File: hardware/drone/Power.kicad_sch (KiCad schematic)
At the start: 48 parts, among them U1 STM32N645I0, U13 LM5907, U3 TPS628303, U4 TPS7A2118PQWDSGRQ1, U5 TPS628303

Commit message: Implemented power mux to select between battery and usb c 5V
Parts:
- added C85: 2.2u, symbol Device:C
- added C86, C89: 100n, symbol Device:C
- added C87, C88: 33u, symbol Device:C
- added L13: 10u, symbol Device:L
- added R15: 53.6k, symbol Device:R
- added R16, R18, R22: 10.2k, symbol Device:R
- added R17: 51.1k, symbol Device:R
- added R19, R21, R23: 5k, symbol Device:R
- added R20: 23.7k, symbol Device:R
- added U16: LMR51635XFDDCR, Package_TO_SOT_SMD:SOT-23-6, symbol SoftDrone:LMR51635XFDDCR
- added U18: TPS2121, Package_TO_SOT_SMD:SOT-583-8, symbol SoftDrone:TPS2121
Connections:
- net GND: now also C85.2, C87.2, C88.2, C89.2, R16.2, R17.2, R19.2, R21.2, R23.2, U16.4 (GND), U18.3 (CP2), U18.9 (ST)
- net VSYS_5V: now also U18.1 (OUT), U18.8 (OUT)
- new net: R17.1, U18.10 (ILM)
- new net: C89.1, U18.11 (SS)
- new net: C86.1, U16.6 (CB)
- new net: C86.2, L13.1, U16.5 (SW)
- new net: R15.2, R16.1, U16.1 (FB)
- new net PMUX_OV1: R20.2, R21.1, U18.5 (OV1)
- new net PMUX_OV2: R22.2, R23.1, U18.4 (OV2)
- new net PMUX_PR1: R18.2, R19.1, U18.6 (PR1)
- new net VBAT: C85.1, U16.2 (EN), U16.3 (VIN)
- new net VSYS_5V_BAT: C87.1, C88.1, L13.2, R15.1, U18.2 (IN2)
- new net VSYS_5V_USBC: R18.1, R20.1, R22.1, U18.7 (IN1)
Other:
- note added: "5V Power Mux"
- moved on the sheet: C10, C11, C12, C13, C14, C15, C16, C17, C18, C19, C2, C20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

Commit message: cleanup
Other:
- note added: "6S VBAT -> 5V SMPS"
- moved on the sheet: C10, C11, C12, C16, C19, C2, C20, C21, C22, C23, C24, C25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

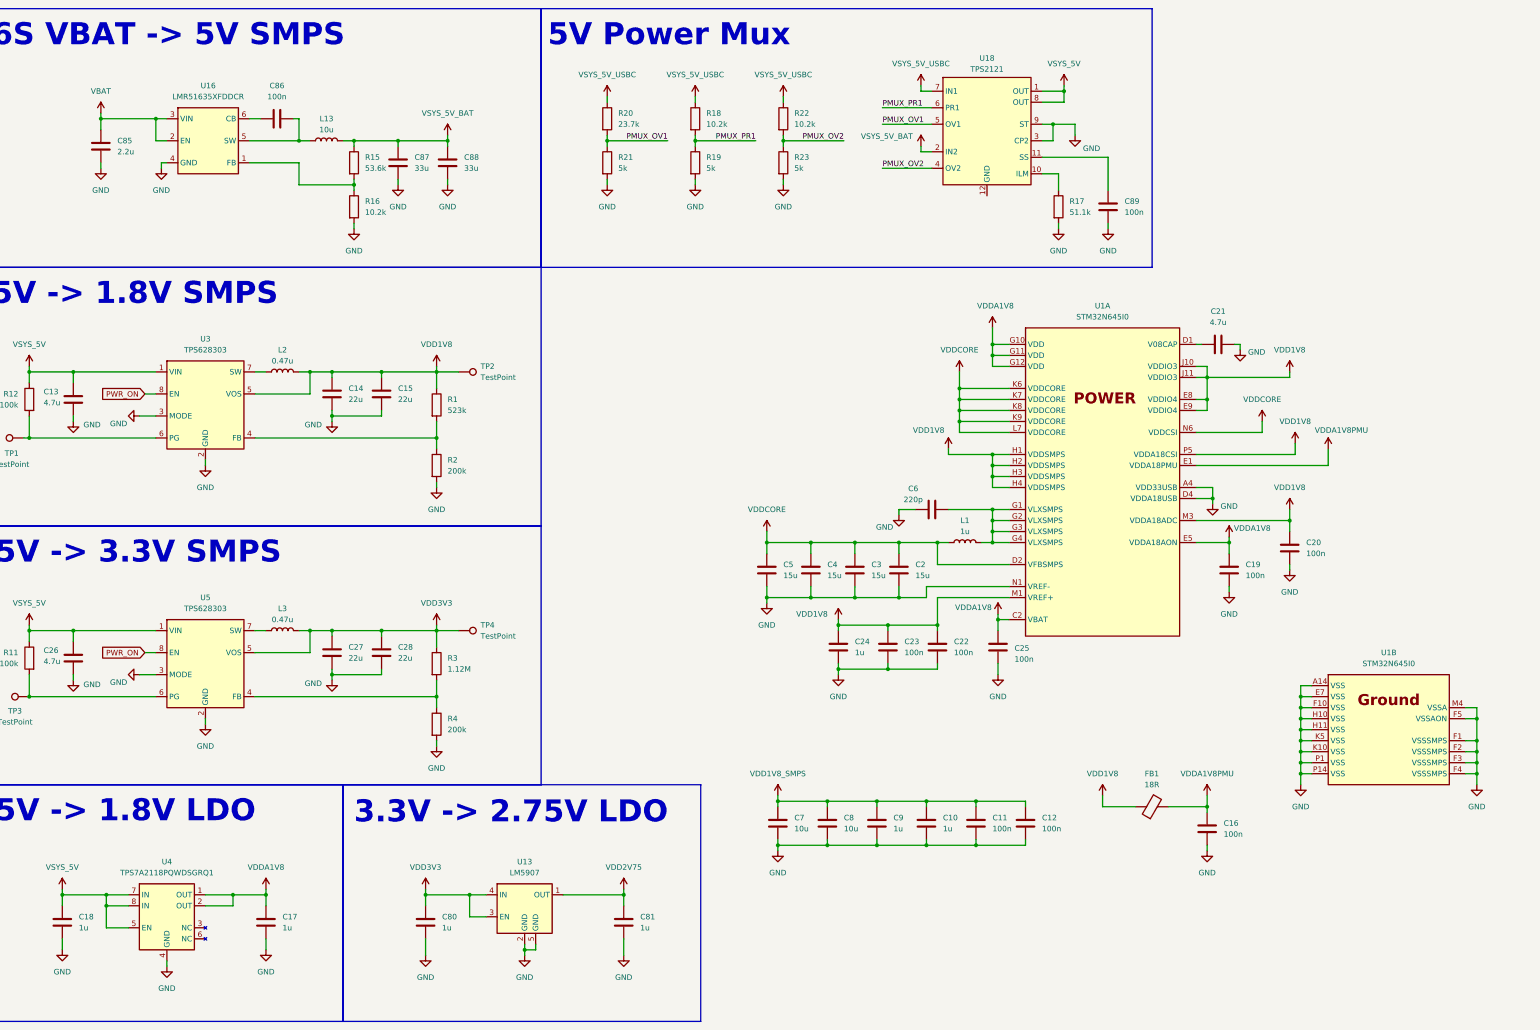
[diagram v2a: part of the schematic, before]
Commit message: Added barometer, more pinmuxxing, added VBAT sensing and reverse voltage protection
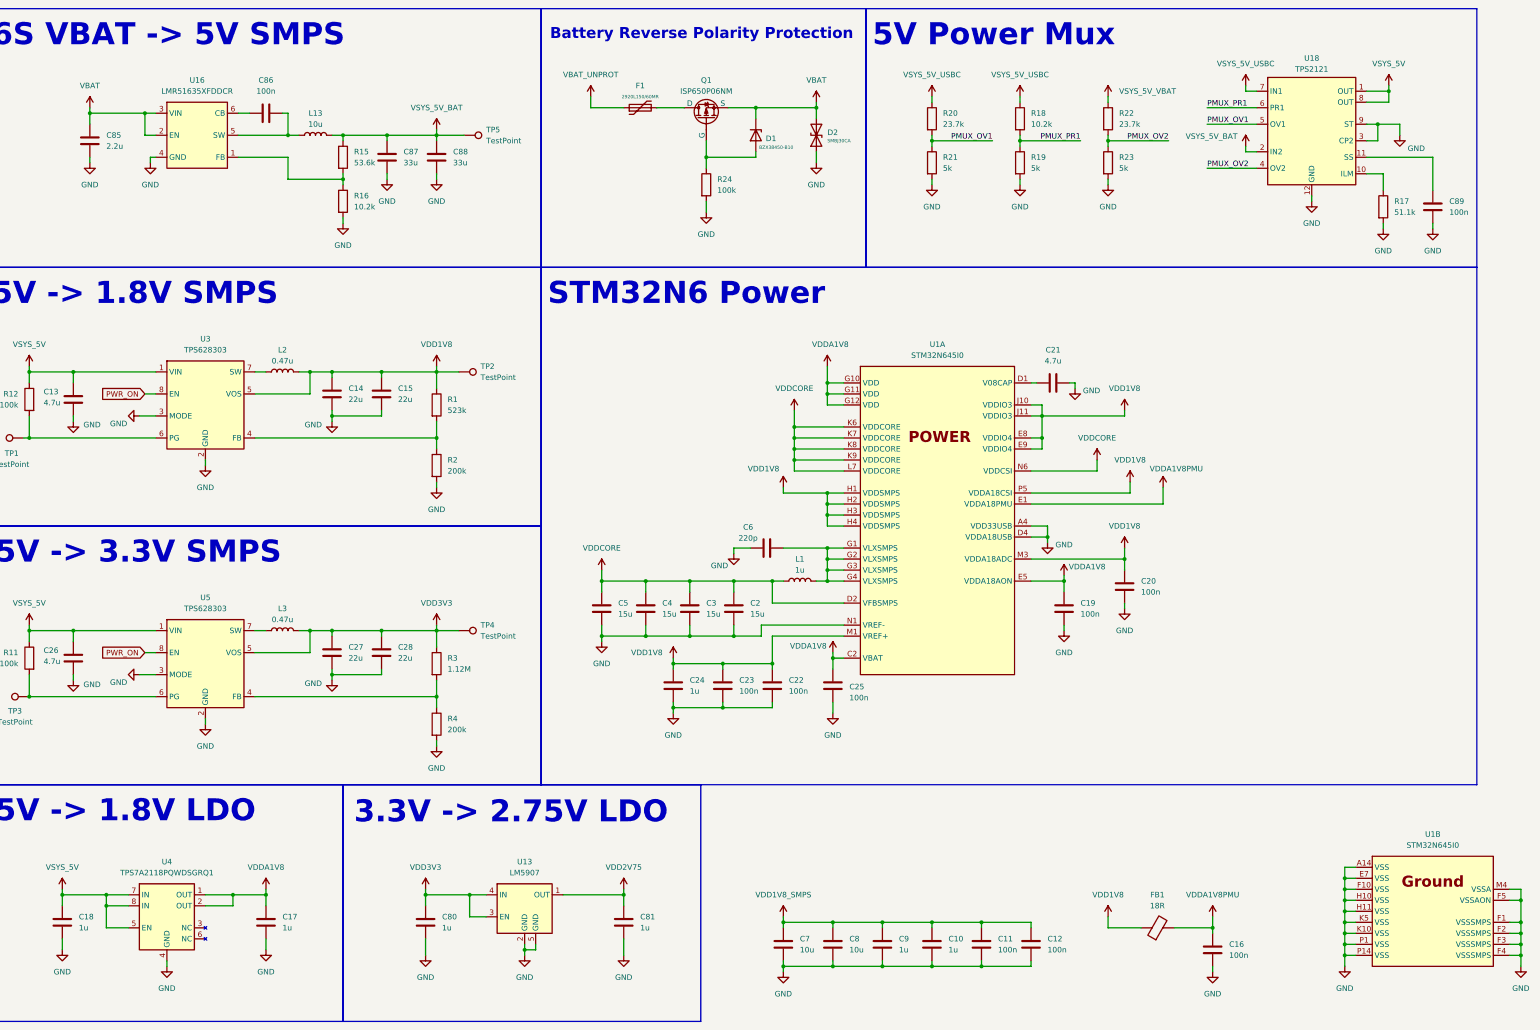
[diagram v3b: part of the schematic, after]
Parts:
- added D1: BZX38450-B10, Package_DIP:DIP-40_W15.24mm, symbol Device:D_Zener
- added D2: SMBJ30CA, Package_DIP:DIP-40_W15.24mm, symbol Device:D_TVS
- added F1: 2920L150/60MR, symbol Device:Polyfuse
- added Q1: ISP650P06NM, Package_DIP:DIP-24_W7.62mm, symbol Simulation_SPICE:PMOS
- added R24: 100k, symbol Device:R
- added TP5: TestPoint, symbol Connector:TestPoint
- R22: value 10.2k -> 23.7k
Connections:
- net GND: now also U18.12 (GND), D2.1 (A1), R24.2
- net VBAT: now also D1.1 (K), D2.2 (A2), Q1.3 (S)
- net VSYS_5V_BAT: now also TP5.1
- net VSYS_5V_USBC: no longer R22.1
- new net: D1.2 (A), Q1.2 (G), R24.1
- new net: F1.2, Q1.1 (D)
- new net VBAT_UNPROT: F1.1
- new net VSYS_5V_VBAT: R22.1
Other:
- note added: "Battery Reverse Polarity Protection"
- note added: "STM32N6 Power"
- moved on the sheet: C10, C11, C12, C16, C19, C2, C20, C21, C22, C23, C24, C25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

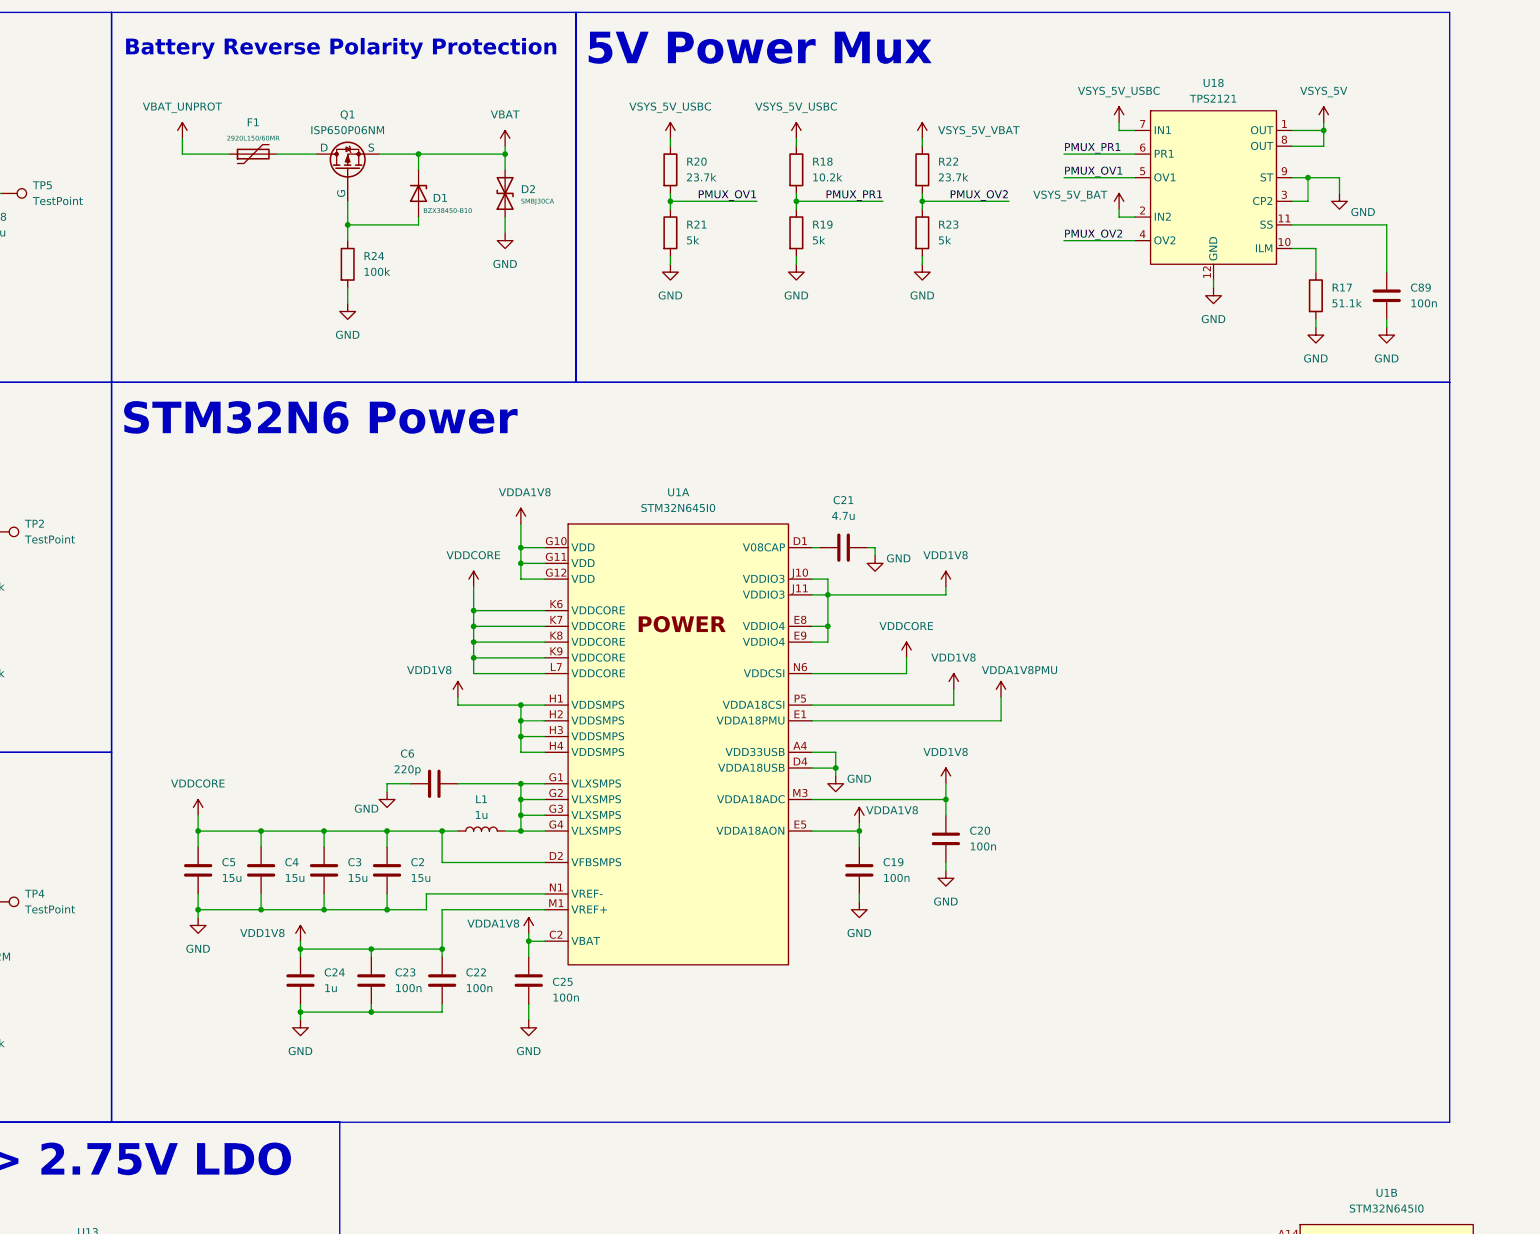
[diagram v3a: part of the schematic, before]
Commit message: Added SWD
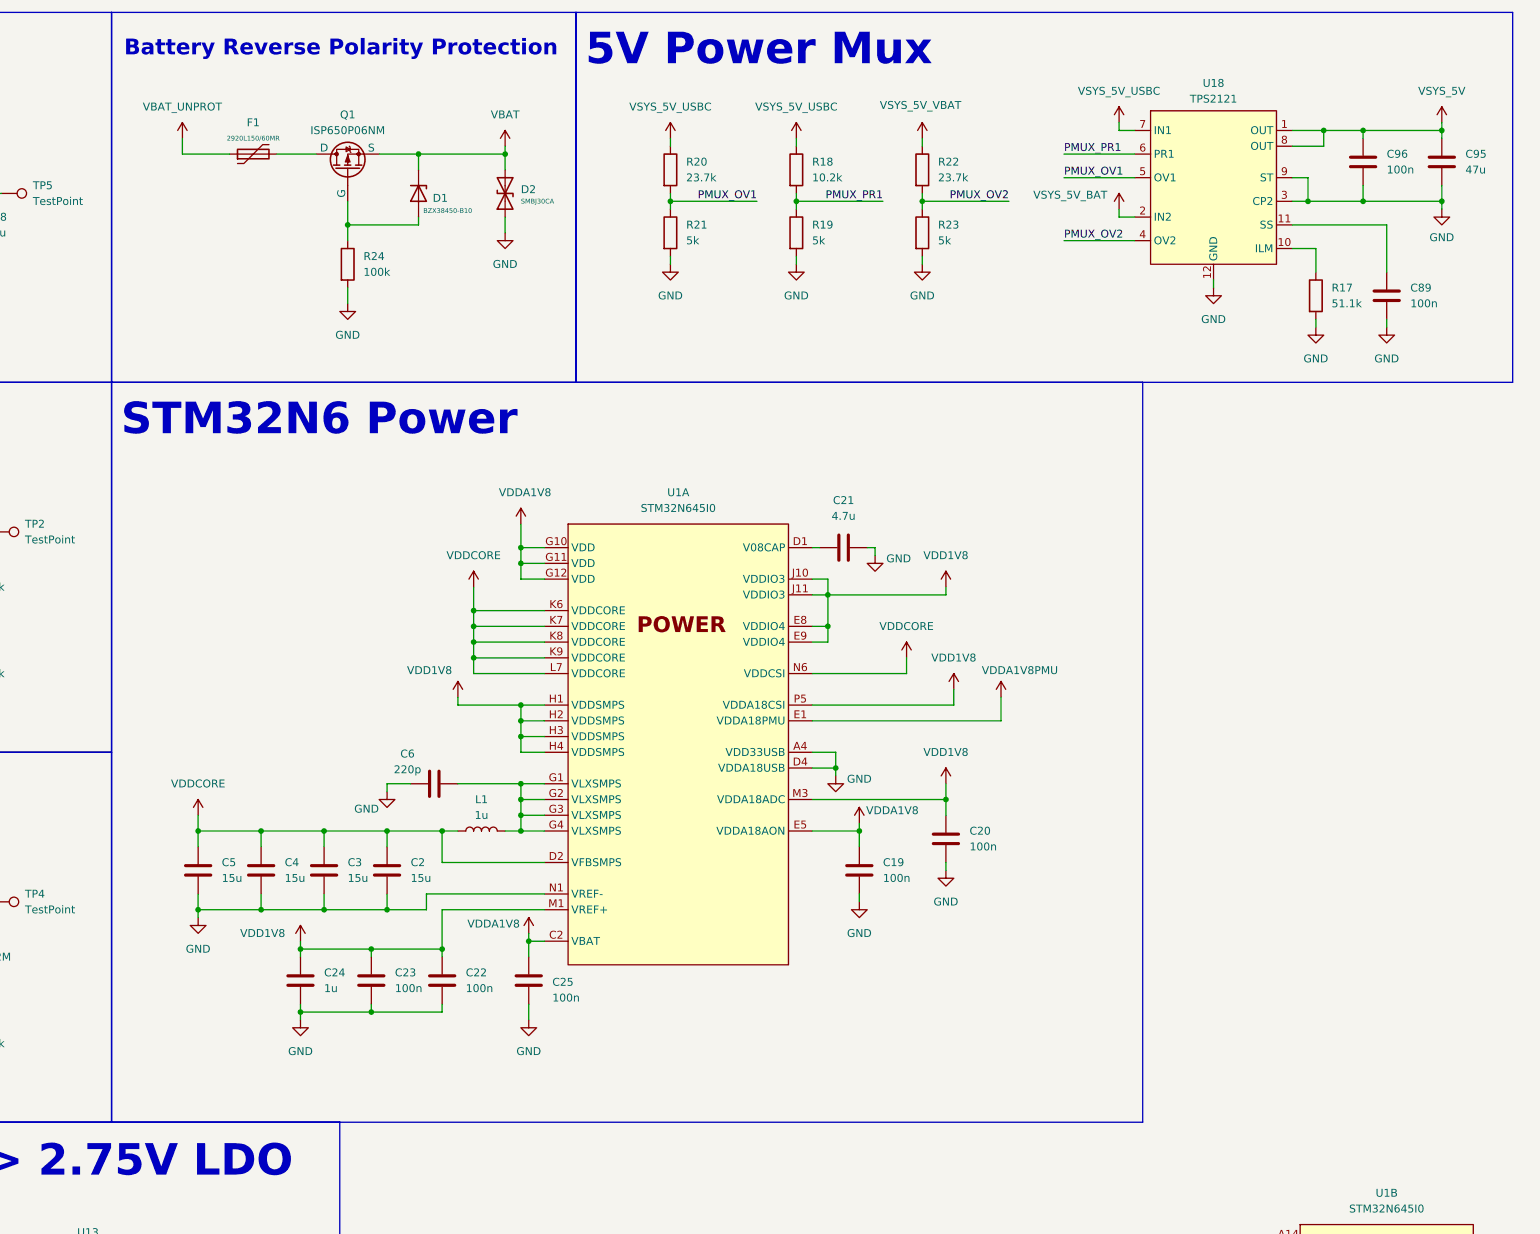
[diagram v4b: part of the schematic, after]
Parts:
- added C95: 47u, symbol Device:C
- added C96: 100n, symbol Device:C
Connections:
- net GND: now also C95.2, C96.2
- net VSYS_5V: now also C95.1, C96.1
